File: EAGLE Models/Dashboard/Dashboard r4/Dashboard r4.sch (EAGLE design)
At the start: 118 parts, among them IC1 AT90CAN128, IC2 MCP2551SO8, IC3 NUP2105L, IC5 FT232RL, Q1 56P2859, U1 74LCX125M

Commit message: Added gerbers, fixed DRCs
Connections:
- removed net BL_CATHODE: CIN13.1, CIN14.1, LCD_CONN.1
- net GND: now also CIN13.1, CIN14.1, LCD_CONN.1
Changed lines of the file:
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@@
 <label x="-205.74" y="50.8" size="1.778" layer="95" rot="R270" xref="yes"/>
+</segment>
+<segment>
+<pinref part="CIN13" gate="G$1" pin="1"/>
+<wire x1="231.14" y1="78.74" x2="231.14" y2="68.58" width="0.1524" layer="91"/>
+<wire x1="231.14" y1="68.58" x2="240.284" y2="68.58" width="0.1524" layer="91"/>
+<pinref part="CIN14" gate="G$1" pin="1"/>
+<wire x1="240.284" y1="68.58" x2="246.38" y2="68.58" width="0.1524" layer="91"/>
+<wire x1="246.38" y1="68.58" x2="269.24" y2="68.58" width="0.1524" layer="91"/>
+<wire x1="246.38" y1="78.74" x2="246.38" y2="68.58" width="0.1524" layer="91"/>
+<junction x="246.38" y="68.58"/>
+<pinref part="GND19" gate="1" pin="GND"/>
+<junction x="240.284" y="68.58"/>
+<label x="269.24" y="68.58" size="1.778" layer="95" xref="yes"/>
+</segment>
+<segment>
+<pinref part="LCD_CONN" gate="A" pin="1"/>
+<wire x1="-508" y1="236.22" x2="-513.08" y2="236.22" width="0.1524" layer="91"/>
+<label x="-513.08" y="236.22" size="1.27" layer="95" rot="R180" xref="yes"/>
 </segment>
 </net>
@@
 </segment>
 </net>
-<net name="BL_CATHODE" class="0">
-<segment>
-<pinref part="LCD_CONN" gate="A" pin="1"/>
-<wire x1="-508" y1="236.22" x2="-513.08" y2="236.22" width="0.1524" layer="91"/>
-<label x="-513.08" y="236.22" size="1.27" layer="95" rot="R180" xref="yes"/>
-</segment>
-<segment>
-<pinref part="CIN13" gate="G$1" pin="1"/>
-<wire x1="231.14" y1="78.74" x2="231.14" y2="68.58" width="0.1524" layer="91"/>
-<wire x1="231.14" y1="68.58" x2="240.284" y2="68.58" width="0.1524" layer="91"/>
-<pinref part="CIN14" gate="G$1" pin="1"/>
-<wire x1="240.284" y1="68.58" x2="246.38" y2="68.58" width="0.1524" layer="91"/>
-<wire x1="246.38" y1="68.58" x2="269.24" y2="68.58" width="0.1524" layer="91"/>
-<wire x1="246.38" y1="78.74" x2="246.38" y2="68.58" width="0.1524" layer="91"/>
-<junction x="246.38" y="68.58"/>
-<pinref part="GND19" gate="1" pin="GND"/>
-<junction x="240.284" y="68.58"/>
-<label x="269.24" y="68.58" size="1.778" layer="95" xref="yes"/>
-</segment>
-</net>

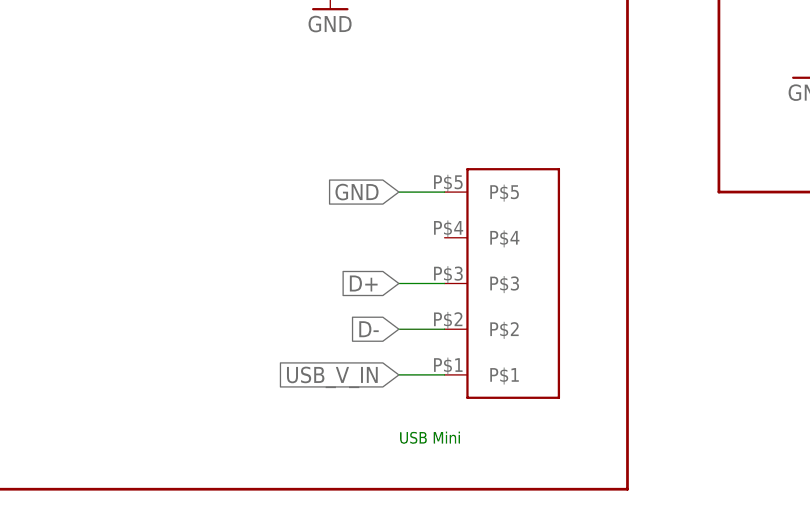
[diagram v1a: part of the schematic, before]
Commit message: Added new mini usb, updated gerber
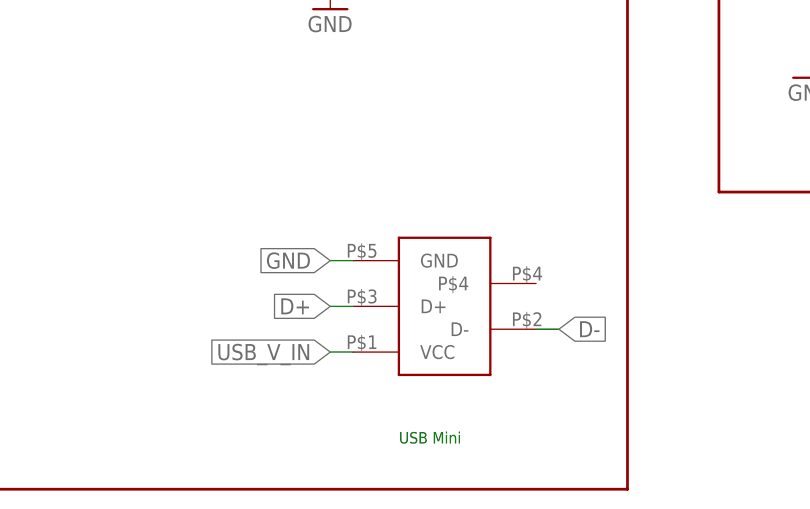
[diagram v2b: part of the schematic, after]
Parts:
- removed U$15: 1734753-1, con-tyco:1734753-1
- added U$1: 1734753-1_MINIUSB_CON, us-te-con:1734753-1_MINIUSB_CON
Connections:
- net D+: now also U$1.D+; no longer U$15.P$3
- net D-: now also U$1.D-; no longer U$15.P$2
- net GND: now also U$1.GND; no longer U$15.P$5
- net USB_V_IN: now also U$1.VCC; no longer U$15.P$1
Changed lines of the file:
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@@
 <part name="F5" library="SparkFun" deviceset="PTC" device="SMD" value="15V,0.5A"/>
 <part name="U$13" library="kyocera" deviceset="TCG043WQLBAANN-GN00" device=""/>
-<part name="U$15" library="con-tyco" library_urn="urn:adsk.eagle:library:192" deviceset="1734753-1" device=""/>
 <part name="U$14" library="DashAndCAN library" deviceset="ROTSWITCH" device=""/>
 <part name="R17" library="rcl" deviceset="R-US_" device="R0603" value="1k"/>
@@
 <part name="C24" library="rcl" deviceset="C-US" device="C0603" value="10uF"/>
 <part name="RCOMM1" library="Vishay_By_element14_Batch_1" deviceset="TNPW12062K00BEEN" device="" value="17.2K"/>
+<part name="U$1" library="us-te-con" deviceset="1734753-1_MINIUSB_CON" device=""/>
 </parts>
 <sheets>
@@
 <instance part="F5" gate="G$1" x="-430.53" y="36.83" rot="R270"/>
 <instance part="U$13" gate="G$1" x="-439.42" y="218.44"/>
-<instance part="U$15" gate="G$1" x="-299.72" y="2.54"/>
 <instance part="U$14" gate="G$1" x="111.76" y="292.1" rot="R90"/>
 <instance part="R17" gate="G$1" x="86.36" y="262.89"/>
@@
 <instance part="C24" gate="G$1" x="-182.88" y="60.96"/>
 <instance part="RCOMM1" gate="A" x="111.76" y="76.2" rot="R90"/>
+<instance part="U$1" gate="G$1" x="-307.34" y="0"/>
 </instances>
 <busses>
@@
 </segment>
 <segment>
-<wire x1="-307.34" y1="12.7" x2="-312.42" y2="12.7" width="0.1524" layer="91"/>
-<label x="-312.42" y="12.7" size="1.778" layer="95" rot="R180" xref="yes"/>
-<pinref part="U$15" gate="G$1" pin="P$5"/>
-</segment>
-<segment>
 <wire x1="162.56" y1="255.27" x2="162.56" y2="284.48" width="0.1524" layer="91"/>
 <wire x1="162.56" y1="284.48" x2="165.1" y2="284.48" width="0.1524" layer="91"/>
@@
 <label x="-513.08" y="236.22" size="1.27" layer="95" rot="R180" xref="yes"/>
 </segment>
+<segment>
+<pinref part="U$1" gate="G$1" pin="GND"/>
+<wire x1="-317.5" y1="5.08" x2="-320.04" y2="5.08" width="0.1524" layer="91"/>
+<label x="-320.04" y="5.08" size="1.778" layer="95" rot="R180" xref="yes"/>
+</segment>
 </net>
 <net name="XTAL1" class="0">
@@
 </segment>
 <segment>
-<wire x1="-307.34" y1="-2.54" x2="-312.42" y2="-2.54" width="0.1524" layer="91"/>
-<label x="-312.42" y="-2.54" size="1.778" layer="95" rot="R180" xref="yes"/>
-<pinref part="U$15" gate="G$1" pin="P$2"/>
+<pinref part="U$1" gate="G$1" pin="D-"/>
+<wire x1="-297.18" y1="-2.54" x2="-294.64" y2="-2.54" width="0.1524" layer="91"/>
+<label x="-294.64" y="-2.54" size="1.778" layer="95" xref="yes"/>
 </segment>
 </net>
@@
 </segment>
 <segment>
-<wire x1="-307.34" y1="2.54" x2="-312.42" y2="2.54" width="0.1524" layer="91"/>
-<label x="-312.42" y="2.54" size="1.778" layer="95" rot="R180" xref="yes"/>
-<pinref part="U$15" gate="G$1" pin="P$3"/>
+<pinref part="U$1" gate="G$1" pin="D+"/>
+<wire x1="-317.5" y1="0" x2="-320.04" y2="0" width="0.1524" layer="91"/>
+<label x="-320.04" y="0" size="1.778" layer="95" rot="R180" xref="yes"/>
 </segment>
 </net>
@@
 <net name="USB_V_IN" class="3">
 <segment>
-<wire x1="-307.34" y1="-7.62" x2="-312.42" y2="-7.62" width="0.1524" layer="91"/>
-<label x="-312.42" y="-7.62" size="1.778" layer="95" rot="R180" xref="yes"/>
-<pinref part="U$15" gate="G$1" pin="P$1"/>
-</segment>
-<segment>
 <pinref part="F1" gate="G$1" pin="2"/>
 <wire x1="-322.58" y1="55.88" x2="-330.2" y2="55.88" width="0.1524" layer="91"/>
 <label x="-330.2" y="55.88" size="1.778" layer="95" rot="R180" xref="yes"/>
 </segment>
-</net>
+<segment>
+<pinref part="U$1" gate="G$1" pin="VCC"/>
+<wire x1="-317.5" y1="-5.08" x2="-320.04" y2="-5.08" width="0.1524" layer="91"/>
+<label x="-320.04" y="-5.08" size="1.778" layer="95" rot="R180" xref="yes"/>
+</segment>
+</net>

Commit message: Mini USB troubleshooting
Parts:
- removed C12: 100n, rcl:C-USC0805
- removed F1: 16V,0.25A, SparkFun:PTCSMD
- removed U$1: 1734753-1_MINIUSB_CON, us-te-con:1734753-1_MINIUSB_CON
- added U$5: 1734753-1_MINIUSB_CON, us-te-con:1734753-1_MINIUSB_CON
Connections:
- removed net USB_V_IN: F1.2, U$1.VCC
- net D+: now also U$5.D+; no longer U$1.D+
- net D-: now also U$5.D-; no longer U$1.D-
- net GND: now also U$5.GND; no longer C12.2, U$1.GND
- net VCC: now also U$5.VCC; no longer C12.1, F1.1
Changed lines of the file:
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@@
 <part name="P+4" library="supply1" library_urn="urn:adsk.eagle:library:371" deviceset="VCC" device=""/>
 <part name="P+5" library="supply1" library_urn="urn:adsk.eagle:library:371" deviceset="VCC" device=""/>
-<part name="C12" library="rcl" library_urn="urn:adsk.eagle:library:334" deviceset="C-US" device="C0805" package3d_urn="urn:adsk.eagle:package:23617/2" value="100n"/>
-<part name="GND15" library="supply1" library_urn="urn:adsk.eagle:library:371" deviceset="GND" device=""/>
 <part name="C18" library="rcl" library_urn="urn:adsk.eagle:library:334" deviceset="C-US" device="C0805" package3d_urn="urn:adsk.eagle:package:23617/2" value="100n"/>
 <part name="GND17" library="supply1" library_urn="urn:adsk.eagle:library:371" deviceset="GND" device=""/>
@@
 <part name="R7" library="rcl" library_urn="urn:adsk.eagle:library:334" deviceset="R-US_" device="R0805" package3d_urn="urn:adsk.eagle:package:23553/2" value="1k"/>
 <part name="P+8" library="supply1" library_urn="urn:adsk.eagle:library:371" deviceset="VCC" device=""/>
-<part name="F1" library="SparkFun" deviceset="PTC" device="SMD" value="16V,0.25A"/>
 <part name="L1" library="rcl" library_urn="urn:adsk.eagle:library:334" deviceset="L-US" device="L3216C" package3d_urn="urn:adsk.eagle:package:23476/2" value="CS321613-100K"/>
 <part name="U$2" library="ftdichip" library_urn="urn:adsk.eagle:library:231" deviceset="FT801" device=""/>
@@
 <part name="C24" library="rcl" deviceset="C-US" device="C0603" value="10uF"/>
 <part name="RCOMM1" library="Vishay_By_element14_Batch_1" deviceset="TNPW12062K00BEEN" device="" value="17.2K"/>
-<part name="U$1" library="us-te-con" deviceset="1734753-1_MINIUSB_CON" device=""/>
+<part name="U$5" library="us-te-con" deviceset="1734753-1_MINIUSB_CON" device=""/>
 </parts>
 <sheets>
@@
 <instance part="P+4" gate="VCC" x="-88.9" y="149.86"/>
 <instance part="P+5" gate="VCC" x="-88.9" y="139.7"/>
-<instance part="C12" gate="G$1" x="-307.34" y="46.863"/>
-<instance part="GND15" gate="1" x="-320.04" y="33.02"/>
 <instance part="C18" gate="G$1" x="-220.98" y="205.74"/>
 <instance part="GND17" gate="1" x="-213.36" y="175.26"/>
@@
 <instance part="R7" gate="G$1" x="-157.48" y="226.06"/>
 <instance part="P+8" gate="VCC" x="-109.22" y="160.02"/>
-<instance part="F1" gate="G$1" x="-314.96" y="55.88" rot="R180"/>
 <instance part="L1" gate="G$1" x="-91.44" y="157.48" rot="R90"/>
 <instance part="U$2" gate="A" x="-327.66" y="203.2"/>
@@
 <instance part="C24" gate="G$1" x="-182.88" y="60.96"/>
 <instance part="RCOMM1" gate="A" x="111.76" y="76.2" rot="R90"/>
-<instance part="U$1" gate="G$1" x="-307.34" y="0"/>
+<instance part="U$5" gate="G$1" x="-309.88" y="0"/>
 </instances>
 <busses>
@@
 </segment>
 <segment>
-<wire x1="-307.34" y1="55.88" x2="-307.34" y2="49.403" width="0.1524" layer="91"/>
-<wire x1="-307.34" y1="55.88" x2="-299.72" y2="55.88" width="0.1524" layer="91"/>
-<wire x1="-309.88" y1="55.88" x2="-307.34" y2="55.88" width="0.1524" layer="91"/>
-<label x="-307.34" y="55.88" size="1.778" layer="95"/>
-<pinref part="C12" gate="G$1" pin="1"/>
-<pinref part="F1" gate="G$1" pin="1"/>
-<junction x="-307.34" y="55.88"/>
-</segment>
-<segment>
 <pinref part="R6" gate="G$1" pin="2"/>
 <wire x1="-266.7" y1="55.88" x2="-266.7" y2="71.12" width="0.1524" layer="91"/>
@@
 <label x="-180.34" y="68.58" size="1.778" layer="95" xref="yes"/>
 <junction x="-182.88" y="68.58"/>
+</segment>
+<segment>
+<pinref part="U$5" gate="G$1" pin="VCC"/>
+<wire x1="-320.04" y1="-5.08" x2="-322.58" y2="-5.08" width="0.1524" layer="91"/>
+<label x="-330.2" y="-5.08" size="1.778" layer="95"/>
 </segment>
 </net>
@@
 </segment>
 <segment>
-<wire x1="-320.04" y1="40.64" x2="-320.04" y2="35.56" width="0.1524" layer="91"/>
-<wire x1="-307.34" y1="41.783" x2="-307.34" y2="40.64" width="0.1524" layer="91"/>
-<wire x1="-320.04" y1="40.64" x2="-307.34" y2="40.64" width="0.1524" layer="91"/>
-<pinref part="GND15" gate="1" pin="GND"/>
-<pinref part="C12" gate="G$1" pin="2"/>
-</segment>
-<segment>
 <pinref part="U$2" gate="A" pin="GND"/>
 <pinref part="GND2" gate="1" pin="GND"/>
@@
 </segment>
 <segment>
-<pinref part="U$1" gate="G$1" pin="GND"/>
-<wire x1="-317.5" y1="5.08" x2="-320.04" y2="5.08" width="0.1524" layer="91"/>
-<label x="-320.04" y="5.08" size="1.778" layer="95" rot="R180" xref="yes"/>
+<pinref part="U$5" gate="G$1" pin="GND"/>
+<wire x1="-320.04" y1="5.08" x2="-322.58" y2="5.08" width="0.1524" layer="91"/>
+<label x="-330.2" y="5.08" size="1.778" layer="95"/>
 </segment>
 </net>
@@
 </segment>
 <segment>
-<pinref part="U$1" gate="G$1" pin="D-"/>
-<wire x1="-297.18" y1="-2.54" x2="-294.64" y2="-2.54" width="0.1524" layer="91"/>
-<label x="-294.64" y="-2.54" size="1.778" layer="95" xref="yes"/>
+<pinref part="U$5" gate="G$1" pin="D-"/>
+<wire x1="-299.72" y1="-2.54" x2="-297.18" y2="-2.54" width="0.1524" layer="91"/>
+<label x="-294.64" y="-2.54" size="1.778" layer="95"/>
 </segment>
 </net>
@@
 </segment>
 <segment>
-<pinref part="U$1" gate="G$1" pin="D+"/>
-<wire x1="-317.5" y1="0" x2="-320.04" y2="0" width="0.1524" layer="91"/>
-<label x="-320.04" y="0" size="1.778" layer="95" rot="R180" xref="yes"/>
+<pinref part="U$5" gate="G$1" pin="D+"/>
+<wire x1="-320.04" y1="0" x2="-322.58" y2="0" width="0.1524" layer="91"/>
+<label x="-327.66" y="0" size="1.778" layer="95"/>
 </segment>
 </net>
@@
 </segment>
 </net>
-<net name="USB_V_IN" class="3">
-<segment>
-<pinref part="F1" gate="G$1" pin="2"/>
-<wire x1="-322.58" y1="55.88" x2="-330.2" y2="55.88" width="0.1524" layer="91"/>
-<label x="-330.2" y="55.88" size="1.778" layer="95" rot="R180" xref="yes"/>
-</segment>
-<segment>
-<pinref part="U$1" gate="G$1" pin="VCC"/>
-<wire x1="-317.5" y1="-5.08" x2="-320.04" y2="-5.08" width="0.1524" layer="91"/>
-<label x="-320.04" y="-5.08" size="1.778" layer="95" rot="R180" xref="yes"/>
-</segment>
-</net>

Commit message: airwire fixes
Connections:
- removed net 12V_PROTECTED: U$10.E, U$12.E, U$8.E
- net 12V: now also U$10.E, U$12.E, U$8.E
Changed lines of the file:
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@@
-</segment>
-</net>
-<net name="12V_PROTECTED" class="3">
-<segment>
-<pinref part="U$8" gate="G$1" pin="E"/>
-<wire x1="-495.3" y1="55.88" x2="-495.3" y2="62.23" width="0.1524" layer="91"/>
-<label x="-495.3" y="62.23" size="1.778" layer="95" rot="R90" xref="yes"/>
-</segment>
-<segment>
-<pinref part="U$10" gate="G$1" pin="E"/>
-<wire x1="-430.53" y1="129.54" x2="-430.53" y2="135.89" width="0.1524" layer="91"/>
-<label x="-430.53" y="135.89" size="1.778" layer="95" rot="R90" xref="yes"/>
-</segment>
-<segment>
-<pinref part="U$12" gate="G$1" pin="E"/>
-<wire x1="-430.53" y1="55.88" x2="-430.53" y2="62.23" width="0.1524" layer="91"/>
-<label x="-430.53" y="62.23" size="1.778" layer="95" rot="R90" xref="yes"/>
 </segment>
 </net>
@@
 <label x="73.66" y="119.38" size="1.778" layer="95" rot="R180" xref="yes"/>
 </segment>
+<segment>
+<pinref part="U$10" gate="G$1" pin="E"/>
+<wire x1="-430.53" y1="129.54" x2="-430.53" y2="135.89" width="0.1524" layer="91"/>
+<label x="-430.53" y="135.89" size="1.778" layer="95" rot="R90" xref="yes"/>
+</segment>
+<segment>
+<pinref part="U$8" gate="G$1" pin="E"/>
+<wire x1="-495.3" y1="55.88" x2="-495.3" y2="62.23" width="0.1524" layer="91"/>
+<label x="-495.3" y="62.23" size="1.778" layer="95" rot="R90" xref="yes"/>
+</segment>
+<segment>
+<pinref part="U$12" gate="G$1" pin="E"/>
+<wire x1="-430.53" y1="55.88" x2="-430.53" y2="62.23" width="0.1524" layer="91"/>
+<label x="-430.53" y="62.23" size="1.778" layer="95" rot="R90" xref="yes"/>
+</segment>
 </net>

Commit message: All components given specific reference designators
All U$n components given updates reference designators
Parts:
- renumbered U$10 to Q3, U$11 to Q6, U$12 to Q7, U$13 to LCD, U$14 to S1, U$16 to S2, U$17 to S3, U$18 to IC7, U$19 to S4, U$2 to IC4, U$20 to S5, U$21 to J2, U$22 to J3, U$23 to J4, U$24 to J5, U$26 to IC8, U$3 to IC6, U$4 to D2, U$5 to J1, U$7 to Q4, U$8 to Q5, U$9 to Q2

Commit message: Renamed ref designators
RCOMM->R
CIN->C
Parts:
- renumbered CIN10 to C10, CIN11 to C11, CIN12 to C12, CIN13 to C3, CIN14 to C4, CIN4 to C5, CIN5 to C15, CIN6 to C6, CIN7 to C17, CIN8 to C21, CIN9 to C22, RCOMM1 to R50, RCOMM2 to R51, RCOMM3 to R52, RCOMM4 to R53
